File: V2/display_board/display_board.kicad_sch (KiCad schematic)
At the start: 48 parts, among them J1 Conn_01x12, J2 Conn_01x12, Q1 Si1308EDL, SW3 SW_Push, SW4 SW_Push, SW5 SW_Push, U1 LTR-303ALS-01, U12 TPS61165DBV, U13 DS18B20Z

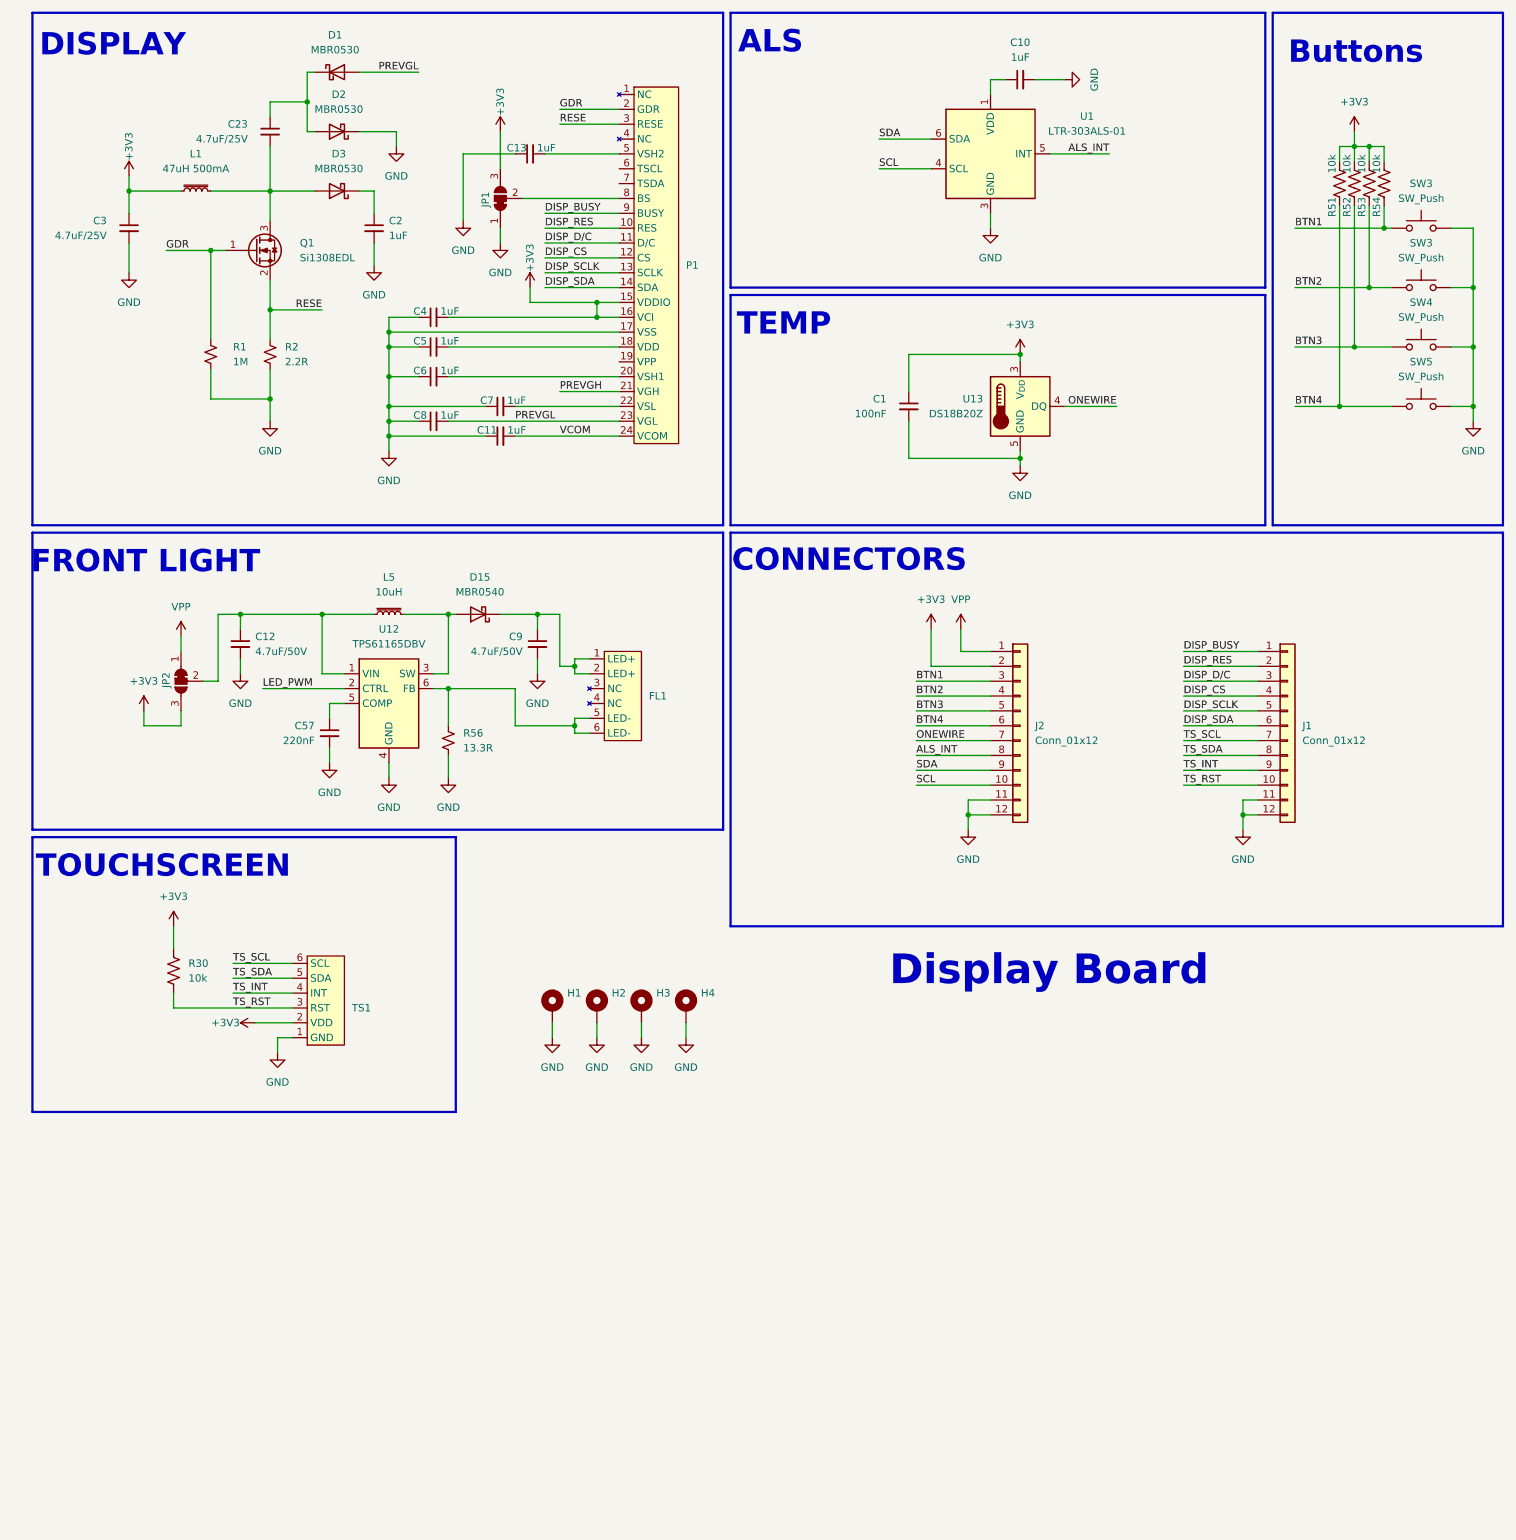
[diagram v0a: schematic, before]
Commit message: Schematic tided up on display board
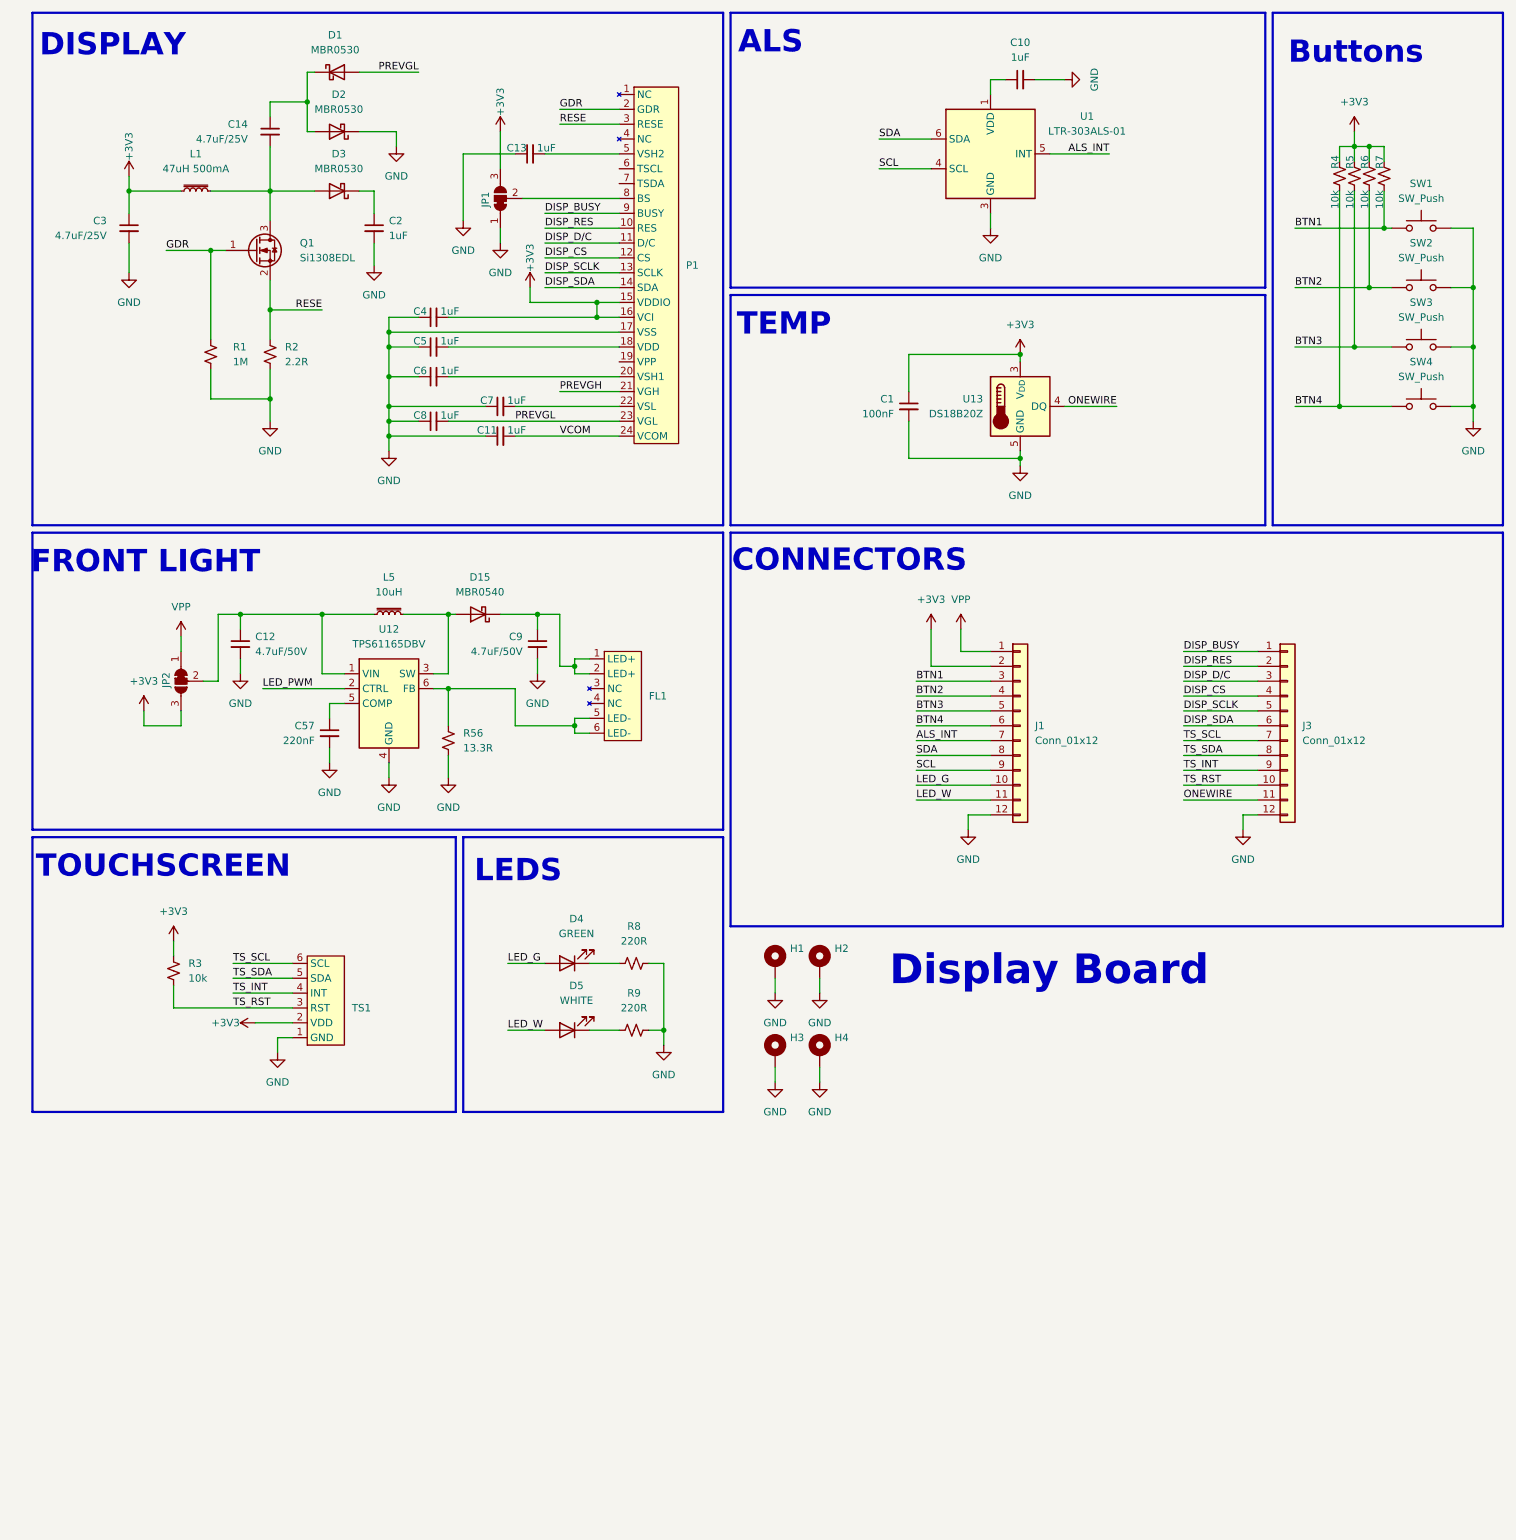
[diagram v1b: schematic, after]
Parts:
- removed C1: 100nF, symbol Device:C_Small
- removed C23: 4.7uF/25V, symbol Device:C_Small
- removed J1: Conn_01x12, Connector_PinHeader_2.54mm:PinHeader_1x12_P2.54mm_Vertical_SMD_Pin1Left, symbol Connector_Generic:Conn_01x12
- removed J2: Conn_01x12, symbol Connector_Generic:Conn_01x12
- removed R30: 10k, symbol Device:R_US
- removed R51, R52, R53, R54: 10k, Resistor_SMD:R_0805_2012Metric, symbol Device:R_US
- removed SW3 (x2), SW4, SW5: SW_Push, Button_Switch_SMD:SW_Push_1P1T_XKB_TS-1187A, symbol Switch:SW_Push
- added C1: 100nF, Capacitor_SMD:C_0603_1608Metric, symbol *partsbox:0603-100nF
- added C14: 4.7uF/25V, Capacitor_SMD:C_0603_1608Metric, symbol *partsbox:0603-4.7uF-25V
- added D4: GREEN, LED_SMD:LED_0805_2012Metric, symbol *partsbox:KT-0805G
- added D5: WHITE, LED_SMD:LED_0805_2012Metric, symbol *partsbox:KT-0805W
- added J1, J3: Conn_01x12, Connector_PinHeader_2.54mm:PinHeader_1x12_P2.54mm_Vertical_SMD_Pin1Left, symbol *partsbox:TSM-112-01-SM-SV
- added R3, R4, R5, R6, R7: 10k, Resistor_SMD:R_0603_1608Metric, symbol *partsbox:0603-10Kohm
- added R8, R9: 220R, Resistor_SMD:R_0603_1608Metric, symbol *partsbox:0603-220ohm
- added SW1, SW2, SW3, SW4: SW_Push, Button_Switch_SMD:SW_Push_1P1T_XKB_TS-1187A, symbol *partsbox:TS-1187A-B-A-B
- H1, H2, H3, H4: footprint (none) -> MountingHole:MountingHole_3.2mm_M3_ISO7380_Pad_TopBottom
- JP1, JP2: footprint (none) -> Jumper:SolderJumper-3_P1.3mm_Bridged12_RoundedPad1.0x1.5mm
- TS1: footprint (none) -> Connector_FFC-FPC:Hirose_FH12-6S-0.5SH_1x06-1MP_P0.50mm_Horizontal
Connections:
- net +3V3: now also C1.1, J1.2 (Pin_2), R3.1, R4.1, R5.1, R6.1, R7.1
- net ALS_INT: now also J1.7 (Pin_7)
- net BTN1: now also J1.3 (Pin_3), R7.2, SW1.1
- net BTN2: now also J1.4 (Pin_4), R6.2, SW2.1
- net BTN3: now also J1.5 (Pin_5), R5.2, SW3.1
- net BTN4: now also J1.6 (Pin_6), R4.2, SW4.1
- net DISP_BUSY: now also J3.1 (Pin_1)
- net DISP_CS: now also J3.4 (Pin_4)
- net DISP_D/C: now also J3.3 (Pin_3)
- net DISP_RES: now also J3.2 (Pin_2)
- net DISP_SCLK: now also J3.5 (Pin_5)
- net DISP_SDA: now also J3.6 (Pin_6)
- net GND: now also C1.2, J1.12 (Pin_12), J3.12 (Pin_12), R8.2, R9.2, SW1.2, SW2.2, SW3.2, SW4.2
- net ONEWIRE: now also J3.11 (Pin_11)
- net SCL: now also J1.9 (Pin_9)
- net SDA: now also J1.8 (Pin_8)
- net TS_INT: now also J3.9 (Pin_9)
- net TS_RST: now also J3.10 (Pin_10), R3.2
- net TS_SCL: now also J3.7 (Pin_7)
- net TS_SDA: now also J3.8 (Pin_8)
- net VPP: now also J1.1 (Pin_1)
- net at D1.1 (K), D2.2 (A): now also C14.1
- net at D3.2 (A), L1.2, Q1.3 (D): now also C14.2
- new net: D4.1 (K), R8.1
- new net: D5.1 (K), R9.1
- new net LED_G: D4.2 (A), J1.10 (Pin_10)
- new net LED_W: D5.2 (A), J1.11 (Pin_11)
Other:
- note added: "LEDS"
- moved on the sheet: H1, H2, H3, H4

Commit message: Main board in progress
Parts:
- renumbered C3 to C1, C13 to C10, C12 to C11, C57 to C12, C9 to C13, C10 to C14, C1 to C15, C14 to C2, C2 to C3, C8 to C7, C7 to C8, C11 to C9, D15 to D4, D4 to D5, D5 to D6, H3 to H2, H2 to H3, J3 to J2, L5 to L2, R7 to R10, R56 to R3, R3 to R4, R8 to R5, R9 to R6, R4 to R7, R5 to R8, R6 to R9, U12 to U1, U1 to U2, U13 to U3
